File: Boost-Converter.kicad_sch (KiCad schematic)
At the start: 20 parts, among them Q3 BSC016N06NS, Q4 BSC016N06NS, U3 LTC3769-QFN

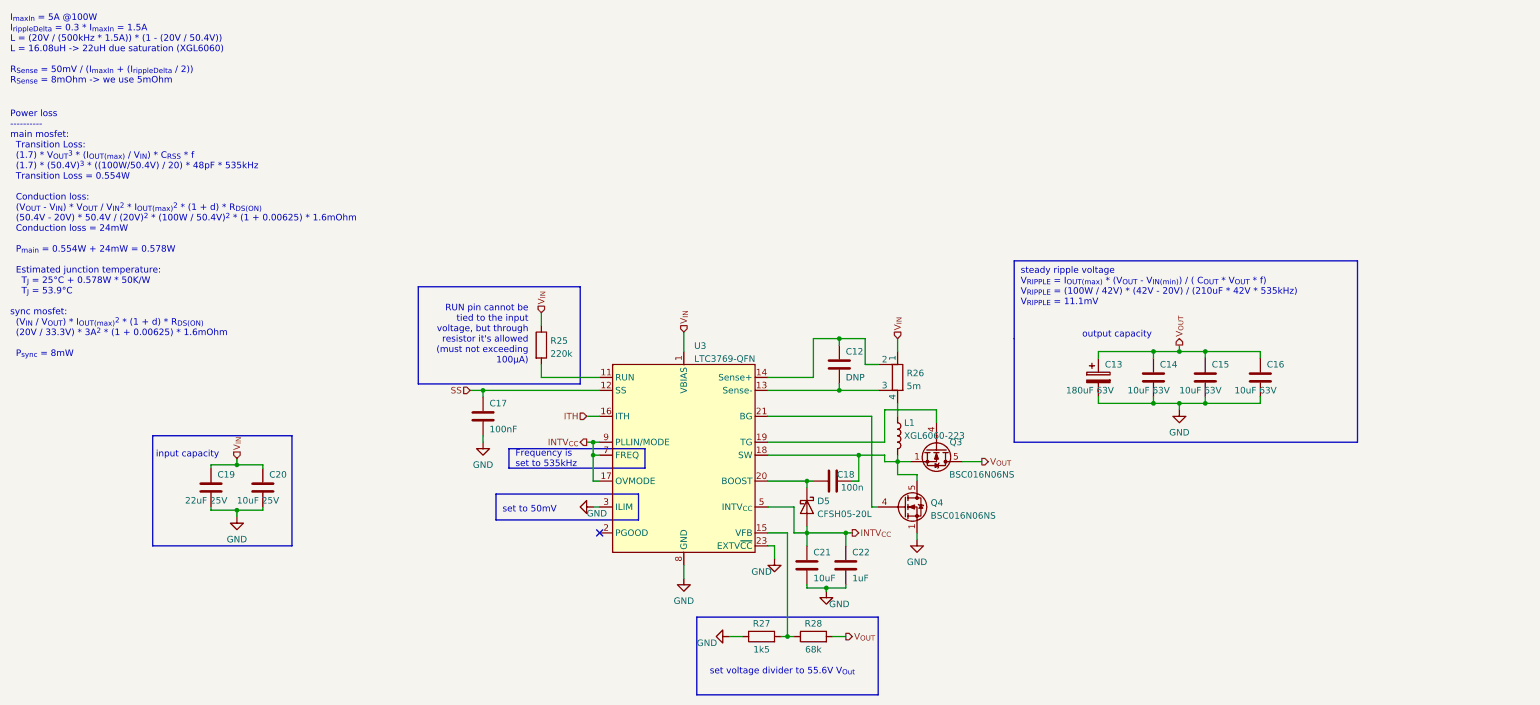
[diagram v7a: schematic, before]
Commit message: Fix wrong battery polarity Enable voltage monitoring at 15V Add caps to OFB and BFB Use another diodes Replace 1206 shunt with 0805 Replace main mosfet with bigger one Improve traces/ground planes
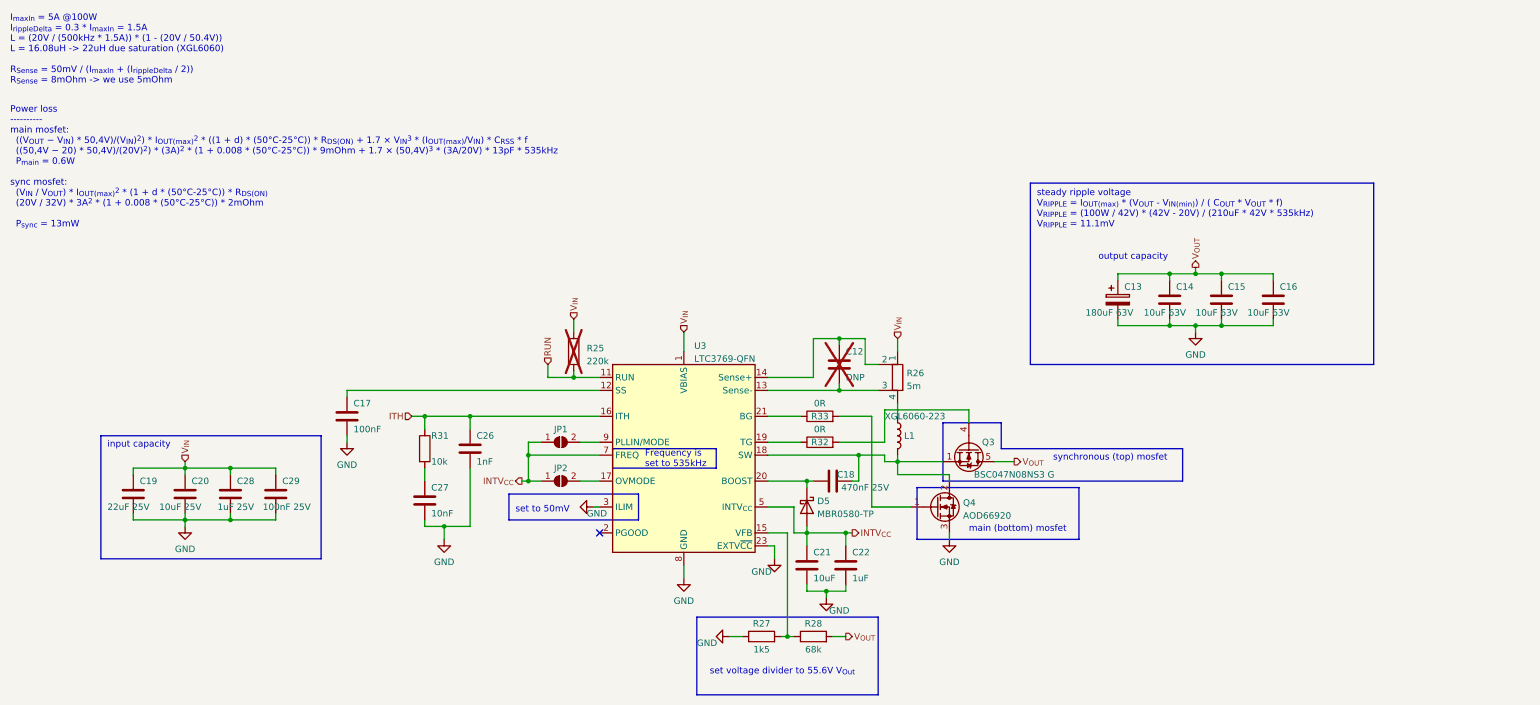
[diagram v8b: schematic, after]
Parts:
- added C26: 1nF, Capacitor_SMD:C_0603_1608Metric, symbol Device:C
- added C27: 10nF, Capacitor_SMD:C_0603_1608Metric, symbol Device:C
- added C28: 1uF 25V, Capacitor_SMD:C_0805_2012Metric, symbol Device:C
- added C29: 100nF 25V, Capacitor_SMD:C_0805_2012Metric, symbol Device:C
- added JP1, JP2: SolderJumper_2_Open, extraFootprints:SolderJumper-Open_0603, symbol Jumper:SolderJumper_2_Open
- added R31: 10k, Resistor_SMD:R_0603_1608Metric, symbol Device:R
- added R32, R33: 0R, Resistor_SMD:R_0603_1608Metric, symbol Device:R
- C12, R25: now not fitted
- C18: value 100n -> 470nF 25V
- D5: value CFSH05-20L -> MBR0580-TP; footprint extraFootprints:SOD882D -> Diode_SMD:D_SOD-123
- L1: footprint Inductor_SMD:L_Coilcraft_XAL60xx_6.36x6.56mm -> Inductor_SMD:L_Coilcraft_XAL6060-XXX
- Q3: value BSC016N06NS -> BSC047N08NS3 G
- Q4: value BSC016N06NS -> AOD66920; footprint Package_TO_SOT_SMD:TDSON-8-1 -> Package_TO_SOT_SMD:TO-252-3_TabPin2; symbol extraSymbols:BSC016N06NS -> Device:Q_NMOS_GDS
- R26: footprint extraFootprints:R_1206_3216Metric_4Kelvin -> extraFootprints:R_0805_2012Metric_4Kelvin
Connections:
- net GND: now also C26.2, C27.2, C28.2, C29.2; no longer Q4.1 (S), Q4.2 (S)
- net INTV_{CC}: now also JP1.1 (A), JP2.1 (A); no longer U3.17 (OVMODE), U3.9 (PLLIN/MODE)
- net ITH: now also C26.1, R31.1
- net V_{IN}: now also C28.1, C29.1
- net at U3.21 (BG): now also R33.1; no longer Q4.4 (G)
- net at C18.1, L1.2, Q3.1 (S)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: now also Q4.2 (D); no longer Q4.5 (D)
- net RUN: now reaches R25.2, U3.11 (RUN)
- net at U3.19 (TG): now also R32.1; no longer Q3.4 (G)
- net SS: no longer names the net of C17.1, U3.12 (SS)
- new net: JP1.2 (B), U3.9 (PLLIN/MODE)
- new net: Q4.1 (G), R33.2
- new net: JP2.2 (B), U3.17 (OVMODE)
- new net: C27.1, R31.2
- new net: Q3.4 (G), R32.2
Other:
- note added: "Power loss ---------- main mosfet: ((V_{OUT} − V_{IN}) * 50,4V)/(V_{IN})^{2}) * I_{OUT(max)}^{2} * ((1 + d) * (50°C-25°C)) * R_{DS(ON)} + 1.7 × V_{IN}^{3} * (I_{OUT(max)}/V_{IN}) * C_{RSS} * f ((50,4V − 20) * 50,4V)/(20V)^{2}) * (3A)^{2} * (1 + 0.008 * (50°C-25°C)) * 9mOhm + 1.7 × (50,4V)^{3} * (3A/20V) * 13pF * 535kHz P_{main} = 0.6W sync mosfet: (V_{IN} / V_{OUT}) * I_{OUT(max)}^{2} * (1 + d * 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"
- note added: "main (bottom) mosfet"
- note added: "synchronous (top) mosfet"
- note removed: "Power loss ---------- main mosfet: Transition Loss: (1.7) * V_{OUT}^{3} * (I_{OUT(max)} / V_{IN}) * C_{RSS} * f (1.7) * (50.4V)^{3} * ((100W/50.4V) / 20) * 48pF * 535kHz Transition Loss = 0.554W Conduction loss: (V_{OUT} - V_{IN}) * V_{OUT} / V_{IN}^{2} * I_{OUT(max)}^{2} * (1 + d) * R_{DS(ON)} (50.4V - 20V) * 50.4V / (20V)^{2} * (100W / 50.4V)^{2} * (1 + 0.00625) * 1.6mOhm Conduction loss = 24mW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"
- note removed: "RUN pin cannot be tied to the input voltage, but through resistor it's allowed (must not exceeding 100µA)"
- moved on the sheet: C13, C14, C15, C16, C17, C19, C20, Q3, Q4
